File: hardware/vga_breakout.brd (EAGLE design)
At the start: 27.9 x 51.7 mm, 11 parts, among them J1 VGA_DB25, J2 HEADER_5P

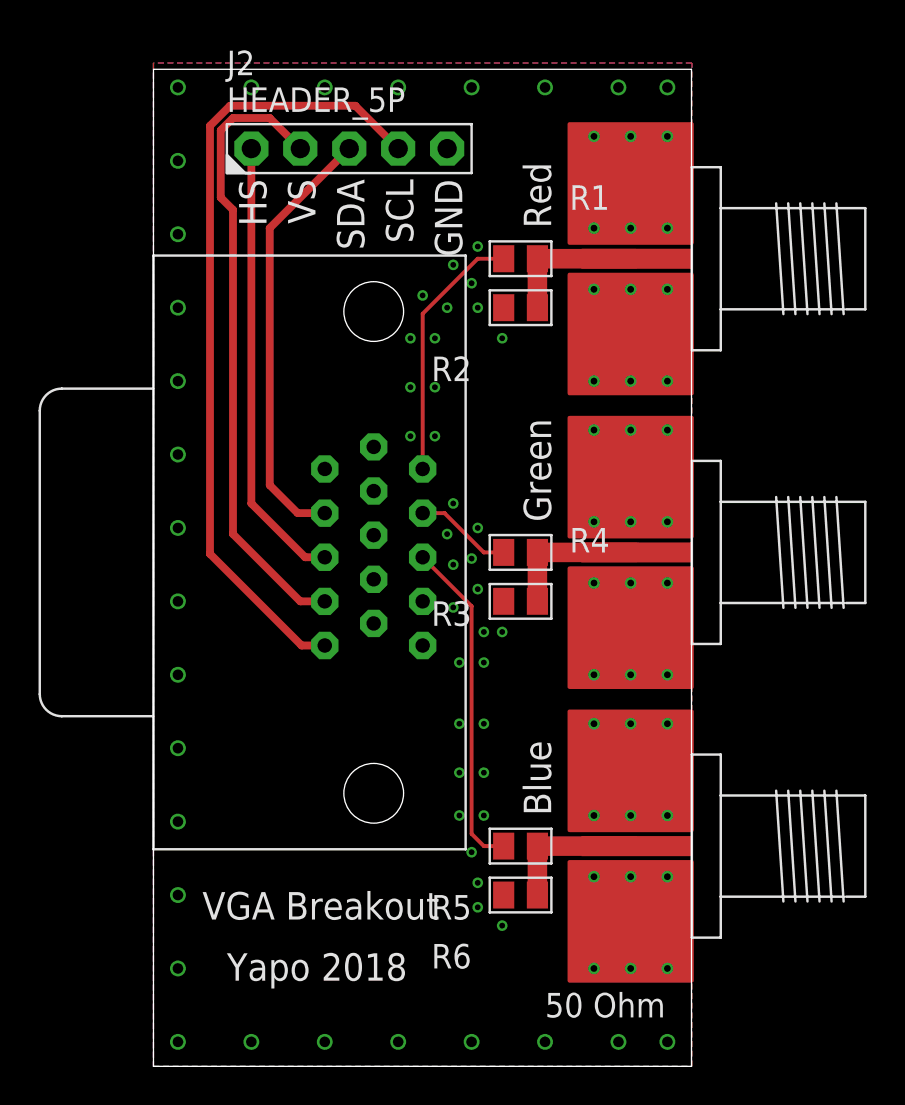
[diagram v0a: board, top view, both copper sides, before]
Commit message: added PTH for VGA connector tabs; LPF has SMA jack
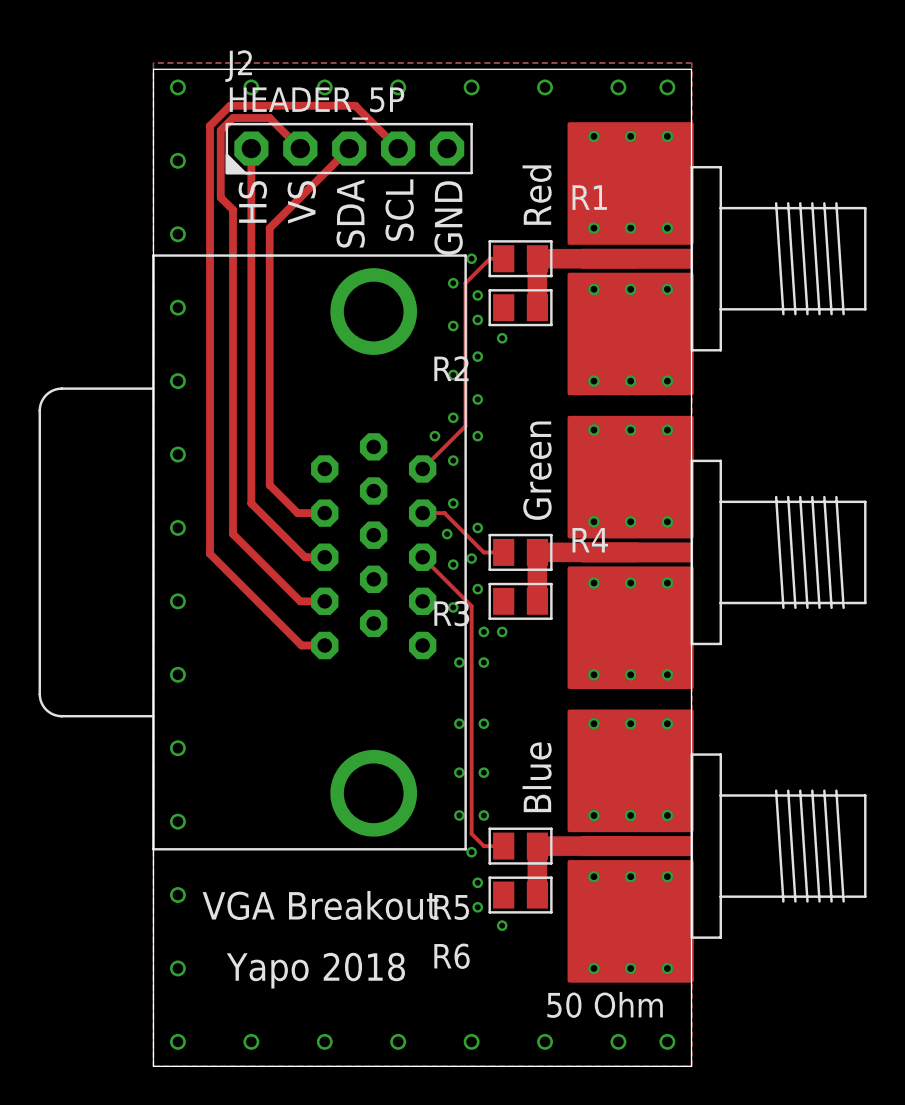
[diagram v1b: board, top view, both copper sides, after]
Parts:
- J1: value VGA_DB25 -> VGA_DB15
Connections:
- net GND: now also J1.TAB@1, J1.TAB@2
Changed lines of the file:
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@@
 <class number="0" name="default" width="0" drill="0">
+</class>
+<class number="1" name="50ohm" width="1.0414" drill="0">
+<clearance class="1" value="0.2032"/>
+</class>
+<class number="2" name="75ohm" width="0.2032" drill="0">
+<clearance class="2" value="0.1524"/>
 </class>
 </classes>
@@
 </autorouter>
 <elements>
-<element name="J1" library="mw-voice-marker" package="VGA_PCB_MALE" value="VGA_DB25" x="11.43" y="26.67" rot="R270"/>
+<element name="J1" library="mw-voice-marker" package="VGA_PCB_MALE" value="VGA_DB15" x="11.43" y="26.67" rot="R270"/>
 <element name="U$1" library="mw-voice-marker" package="EDGE_LAUNCH_RF_CON" value="EDGE_LAUNCH_JACK" x="27.94" y="41.91"/>
 <element name="U$2" library="mw-voice-marker" package="EDGE_LAUNCH_RF_CON" value="EDGE_LAUNCH_JACK" x="27.94" y="26.67"/>
@@
 <via x="26.67" y="50.8" extent="1-16" drill="0.55"/>
 <via x="26.67" y="1.27" extent="1-16" drill="0.55"/>
-<via x="14.605" y="32.7025" extent="1-16" drill="0.3"/>
-<via x="13.335" y="32.7025" extent="1-16" drill="0.3"/>
-<via x="13.335" y="35.2425" extent="1-16" drill="0.3"/>
-<via x="14.605" y="35.2425" extent="1-16" drill="0.3"/>
-<via x="14.605" y="37.7825" extent="1-16" drill="0.3"/>
-<via x="13.335" y="37.7825" extent="1-16" drill="0.3"/>
-<via x="13.97" y="40.005" extent="1-16" drill="0.3"/>
-<via x="15.24" y="39.37" extent="1-16" drill="0.3"/>
-<via x="15.5575" y="41.5925" extent="1-16" drill="0.3"/>
-<via x="16.51" y="40.64" extent="1-16" drill="0.3"/>
-<via x="16.8275" y="42.545" extent="1-16" drill="0.3"/>
-<via x="16.8275" y="39.37" extent="1-16" drill="0.3"/>
-<via x="18.0975" y="37.7825" extent="1-16" drill="0.3"/>
 <via x="18.0975" y="22.5425" extent="1-16" drill="0.3"/>
 <via x="15.5575" y="29.21" extent="1-16" drill="0.3"/>
@@
 <via x="16.8275" y="8.255" extent="1-16" drill="0.3"/>
 <via x="18.0975" y="7.3025" extent="1-16" drill="0.3"/>
+<contactref element="J1" pad="TAB@1"/>
+<contactref element="J1" pad="TAB@2"/>
+<via x="16.8275" y="38.735" extent="1-16" drill="0.3"/>
+<via x="16.8275" y="40.005" extent="1-16" drill="0.3"/>
+<via x="15.5575" y="31.4325" extent="1-16" drill="0.3"/>
+<via x="14.605" y="32.7025" extent="1-16" drill="0.3"/>
+<via x="15.5575" y="33.655" extent="1-16" drill="0.3"/>
+<via x="16.8275" y="32.7025" extent="1-16" drill="0.3"/>
+<via x="16.8275" y="34.6075" extent="1-16" drill="0.3"/>
+<via x="15.5575" y="35.8775" extent="1-16" drill="0.3"/>
+<via x="16.8275" y="36.83" extent="1-16" drill="0.3"/>
+<via x="15.5575" y="38.4175" extent="1-16" drill="0.3"/>
+<via x="15.5575" y="40.64" extent="1-16" drill="0.3"/>
+<via x="16.51" y="41.91" extent="1-16" drill="0.3"/>
+<via x="18.0975" y="37.7825" extent="1-16" drill="0.3"/>
 </signal>
 <signal name="SDA">
@@
 <wire x1="19.925" y1="8.89" x2="19.925" y2="11.43" width="1.016" layer="1"/>
 </signal>
-<signal name="N$2">
+<signal name="N$2" class="1">
 <contactref element="R3" pad="P$1"/>
 <contactref element="U$2" pad="CENTER"/>
@@
 <wire x1="19.925" y1="24.13" x2="19.925" y2="26.67" width="1.016" layer="1"/>
 </signal>
-<signal name="N$3">
+<signal name="N$3" class="1">
 <contactref element="U$1" pad="CENTER"/>
 <contactref element="R1" pad="P$2"/>
@@
 <wire x1="19.925" y1="39.37" x2="19.925" y2="41.91" width="1.016" layer="1"/>
 </signal>
-<signal name="RED">
+<signal name="RED" class="2">
 <contactref element="R1" pad="P$1"/>
 <contactref element="J1" pad="1"/>
-<wire x1="13.97" y1="31" x2="13.97" y2="39.0525" width="0.2032" layer="1"/>
-<wire x1="13.97" y1="39.0525" x2="16.8275" y2="41.91" width="0.2032" layer="1"/>
-<wire x1="16.8275" y1="41.91" x2="18.175" y2="41.91" width="0.2032" layer="1"/>
-</signal>
-<signal name="GREEN">
+<wire x1="13.97" y1="31" x2="16.1925" y2="33.2225" width="0.2032" layer="1"/>
+<wire x1="16.1925" y1="33.2225" x2="16.1925" y2="40.64" width="0.2032" layer="1"/>
+<wire x1="16.1925" y1="40.64" x2="17.4625" y2="41.91" width="0.2032" layer="1"/>
+<wire x1="17.4625" y1="41.91" x2="18.175" y2="41.91" width="0.2032" layer="1"/>
+</signal>
+<signal name="GREEN" class="2">
 <contactref element="J1" pad="2"/>
 <contactref element="R3" pad="P$2"/>
@@
 <wire x1="17.145" y1="26.67" x2="18.175" y2="26.67" width="0.2032" layer="1"/>
 </signal>
-<signal name="BLUE">
+<signal name="BLUE" class="2">
 <contactref element="R5" pad="P$2"/>
 <contactref element="J1" pad="3"/>

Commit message: updated VGA connector footprint
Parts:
- U$1, U$2, U$3: value EDGE_LAUNCH_JACK -> (none)
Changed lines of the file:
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@@
 <elements>
 <element name="J1" library="mw-voice-marker" package="VGA_PCB_MALE" value="VGA_DB15" x="11.43" y="26.67" rot="R270"/>
-<element name="U$1" library="mw-voice-marker" package="EDGE_LAUNCH_RF_CON" value="EDGE_LAUNCH_JACK" x="27.94" y="41.91"/>
-<element name="U$2" library="mw-voice-marker" package="EDGE_LAUNCH_RF_CON" value="EDGE_LAUNCH_JACK" x="27.94" y="26.67"/>
-<element name="U$3" library="mw-voice-marker" package="EDGE_LAUNCH_RF_CON" value="EDGE_LAUNCH_JACK" x="27.94" y="11.43"/>
+<element name="U$1" library="mw-voice-marker" package="EDGE_LAUNCH_RF_CON" value="" x="27.94" y="41.91"/>
+<element name="U$2" library="mw-voice-marker" package="EDGE_LAUNCH_RF_CON" value="" x="27.94" y="26.67"/>
+<element name="U$3" library="mw-voice-marker" package="EDGE_LAUNCH_RF_CON" value="" x="27.94" y="11.43"/>
 <element name="R2" library="mw-voice-marker" package="R0805" value="86.6" x="19.05" y="39.37" rot="R180"/>
 <element name="R1" library="mw-voice-marker" package="R0805" value="43.2" x="19.05" y="41.91"/>
@@
 <contactref element="U$3" pad="CENTER"/>
 <contactref element="R6" pad="P$1"/>
-<wire x1="25.065" y1="11.43" x2="19.925" y2="11.43" width="1.016" layer="1"/>
-<wire x1="19.925" y1="8.89" x2="19.925" y2="11.43" width="1.016" layer="1"/>
+<wire x1="25.065" y1="11.43" x2="19.925" y2="11.43" width="1.0414" layer="1"/>
+<wire x1="19.925" y1="8.89" x2="19.925" y2="11.43" width="1.0414" layer="1"/>
 </signal>
 <signal name="N$2" class="1">
@@
 <contactref element="U$2" pad="CENTER"/>
 <contactref element="R4" pad="P$2"/>
-<wire x1="25.065" y1="26.67" x2="19.925" y2="26.67" width="1.016" layer="1"/>
-<wire x1="19.925" y1="24.13" x2="19.925" y2="26.67" width="1.016" layer="1"/>
+<wire x1="19.925" y1="26.67" x2="25.065" y2="26.67" width="1.0414" layer="1"/>
+<wire x1="19.925" y1="26.67" x2="19.925" y2="24.13" width="1.0414" layer="1"/>
 </signal>
 <signal name="N$3" class="1">
@@
 <contactref element="R1" pad="P$2"/>
 <contactref element="R2" pad="P$1"/>
-<wire x1="25.065" y1="41.91" x2="19.925" y2="41.91" width="1.016" layer="1"/>
-<wire x1="19.925" y1="39.37" x2="19.925" y2="41.91" width="1.016" layer="1"/>
+<wire x1="19.925" y1="41.91" x2="25.065" y2="41.91" width="1.0414" layer="1"/>
+<wire x1="19.925" y1="39.37" x2="19.925" y2="41.91" width="1.0414" layer="1"/>
 </signal>
 <signal name="RED" class="2">

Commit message: reduced breakout board to fit in 5cm
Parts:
- moved J1 1.91 mm to (11.4, 24.8)
- moved J2 1.91 mm to (10.2, 45.7)
- moved R3 1.91 mm to (19.1, 24.8)
- moved U$2 1.91 mm to (27.9, 24.8)
- moved R6 1.91 mm to (19.1, 6.99)
- moved R5 1.90 mm to (19.1, 9.53)
- moved U$3 1.90 mm to (27.9, 9.53)
- moved R4 1.90 mm to (19.1, 22.2)
- moved R1 1.90 mm to (19.1, 40.0)
- moved R2 1.90 mm to (19.1, 37.5)
- moved U$1 1.90 mm to (27.9, 40.0)
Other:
- board size 27.9 x 51.7 mm -> 27.9 x 49.8 mm
- board text removed: "50 Ohm"
